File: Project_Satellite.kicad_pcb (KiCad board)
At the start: 2 copper layers, 40.2 x 65.5 mm, 83 parts, among them J1 Conn_01x02_Socket, J10 Conn_01x01_Socket, J11 Conn_01x01_Socket, J12 Conn_01x01_Socket, J13 Conn_01x01_Socket, J14 Conn_01x01_Socket, J15 Conn_01x01_Socket, J16 Conn_01x01_Socket, J17 Conn_01x01_Socket, J18 Conn_01x01_Socket, J19 Conn_01x01_Socket, J2 Conn_01x01_Socket, J20 Conn_01x01_Socket, J21 Conn_01x01_Socket, J22 Conn_01x01_Socket, J23 Conn_01x01_Socket, J24 Conn_01x01_Socket, J25 Conn_01x03_Socket, J26 Conn_01x03_Socket, J27 Conn_01x03_Socket, J28 Conn_01x03_Socket, J3 Conn_01x01_Socket, J4 Conn_01x01_Socket, J5 Conn_01x02_Socket, J6 Conn_01x02_Socket, J7 Conn_01x01_Socket, J8 Conn_01x02_Socket, J9 Conn_01x02_Socket, U3 TPS62933, U4 RASPBERRY_PI_ZERO_2_W, U5 TLV320AIC3254IRHBR, U6 MEMSMic, U7 MEMSMic, U8 TPA3118D2DAPR

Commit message: TPA3118 changes
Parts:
- removed C11: 0.1uF, Capacitor_SMD:C_0805_2012Metric_Pad1.18x1.45mm_HandSolder
- removed C7: 10uF, Capacitor_SMD:C_1206_3216Metric_Pad1.33x1.80mm_HandSolder
- removed C9: 22uF, Capacitor_SMD:C_1206_3216Metric_Pad1.33x1.80mm_HandSolder
- removed J10, J11, J12, J13, J14, J15, J16, J17, J18, J19, J2, J20, J21, J22, J23, J24, J3, J4, J7: Conn_01x01_Socket, Connector_PinHeader_2.54mm:PinHeader_1x01_P2.54mm_Vertical
- removed J27, J28: Conn_01x03_Socket, Connector_PinHeader_2.54mm:PinHeader_1x03_P2.54mm_Vertical
- removed J5, J6: Conn_01x02_Socket, Connector_PinHeader_2.54mm:PinHeader_1x02_P2.54mm_Vertical
- removed R3: 50, Resistor_SMD:R_0805_2012Metric_Pad1.20x1.40mm_HandSolder
- removed R5, R7: 10k, Resistor_SMD:R_1206_3216Metric_Pad1.30x1.75mm_HandSolder
- removed U6, U7: MEMSMic, MyFootprints:MEMSMic
- added TP2: TestPoint, TestPoint:TestPoint_Pad_D1.0mm, F.Cu at (102.2, 64.0)
- added TP3: TestPoint, TestPoint:TestPoint_Pad_D1.0mm, B.Cu at (101.0, 75.5)
- added TP4: TestPoint, TestPoint:TestPoint_Pad_D1.0mm, B.Cu at (102.2, 64.0)
- added TP5: TestPoint, TestPoint:TestPoint_Pad_D1.0mm, F.Cu at (101.0, 75.5)
- C1, C13, C19, C22, C29, C33, C34, C8, L4, L5: moved to B.Cu
- C10: value 22uF -> 47uF
- C14, C30, C31, C35, C36, C37, C38, C5, C6: moved to F.Cu
- D1: footprint Connector_PinHeader_2.54mm:PinHeader_1x02_P2.54mm_Horizontal -> LED_THT:LED_D3.0mm; moved to F.Cu
- J1, J8, J9: footprint Connector_PinHeader_2.54mm:PinHeader_1x02_P2.54mm_Vertical -> Connector_JST:JST_XH_B2B-XH-A_1x02_P2.50mm_Vertical
- J25, J26: footprint Connector_PinHeader_2.54mm:PinHeader_1x03_P2.54mm_Vertical -> Connector_JST:JST_XH_B3B-XH-A_1x03_P2.50mm_Vertical
- TP1: footprint Connector_PinHeader_2.54mm:PinHeader_1x01_P2.54mm_Horizontal -> TestPoint:TestPoint_Pad_D1.0mm
- U4: footprint Connector_PinHeader_2.54mm:PinHeader_2x20_P2.54mm_Vertical -> Connector_PinSocket_2.54mm:PinSocket_2x20_P2.54mm_Vertical
- moved J9 82.9 mm to (109.4, 115.8), turned to 0 degrees
- moved J8 78.7 mm to (100.9, 115.8), turned to 0 degrees
- moved C36 72.4 mm to (108.3, 109.8), turned to 0 degrees
- moved C37 68.4 mm to (105.4, 110.3)
- moved L3 66.9 mm to (109.4, 103.9), turned to -90 degrees
- moved C38 66.8 mm to (112.9, 110.3)
- moved C1 64.7 mm to (130.5, 67.0), turned to 180 degrees
- moved L4 63.6 mm to (103.4, 106.8), turned to -90 degrees
- moved L5 62.0 mm to (110.9, 106.8), turned to -90 degrees
- moved C35 56.8 mm to (101.4, 109.3), turned to 0 degrees
- moved C33 55.1 mm to (112.9, 96.8), turned to 180 degrees
- moved C8 53.4 mm to (103.8, 73.4), turned to -90 degrees
- moved C5 51.2 mm to (106.2, 73.0), turned to 180 degrees
- moved R2 51.0 mm to (109.0, 70.2), turned to 0 degrees
- moved L2 50.9 mm to (101.9, 103.8), turned to -90 degrees
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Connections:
- C1 pad 1: +15V -> +5V
- C12 pad 2: +3V3 -> +3.3V
- R2 pad 2: Net-(U3-FB) -> +5V
- TP1 pad 1: Net-(U5-MCLK) -> +5V
- U3 pad 2: Net-(J15-Pin_1) -> unconnected-(U3-EN-Pad2)
- U4 pad 1: +3V3 -> +3.3V
- U4 pad 11: Net-(J19-Pin_1) -> /SDZ
- U4 pad 13: Net-(J24-Pin_1) -> unconnected-(U4-GPIO27/GPIO_GEN2-Pad13)
- U4 pad 15: Net-(J20-Pin_1) -> /MUTE
- U4 pad 16: Net-(J21-Pin_1) -> /FAULTZ
- U4 pad 18: Net-(J22-Pin_1) -> unconnected-(U4-GPIO24/GPIO_GEN5-Pad18)
- U4 pad 24: Net-(J14-Pin_1) -> unconnected-(U4-GPIO8/SPI_~{CE0}-Pad24)
- U4 pad 26: Net-(J13-Pin_1) -> unconnected-(U4-GPIO7/SPI_~{CE1}-Pad26)
- U4 pad 29: Net-(J3-Pin_1) -> unconnected-(U4-GPIO5-Pad29)
- U4 pad 3: Net-(J5-Pin_2) -> /SDA
- U4 pad 31: Net-(J4-Pin_1) -> unconnected-(U4-GPIO6-Pad31)
- U4 pad 32: Net-(J16-Pin_1) -> unconnected-(U4-GPIO12-Pad32)
- U4 pad 33: Net-(J17-Pin_1) -> unconnected-(U4-GPIO13-Pad33)
- U4 pad 36: Net-(J18-Pin_1) -> /RESET
- U4 pad 37: Net-(J23-Pin_1) -> unconnected-(U4-GPIO26-Pad37)
- U4 pad 5: Net-(J5-Pin_1) -> /SCL
- U4 pad 7: Net-(J2-Pin_1) -> unconnected-(U4-GPIO4/GPIO_GCLK-Pad7)
- U5 pad 1: Net-(U5-MCLK) -> unconnected-(U5-MCLK-Pad1)
- U5 pad 10: Net-(J6-Pin_1) -> /SDA
- U5 pad 31: Net-(J7-Pin_1) -> /RESET
- U5 pad 9: Net-(J6-Pin_2) -> /SCL
- U8 pad 12: Net-(J12-Pin_1) -> /MUTE
- U8 pad 2: Net-(J10-Pin_1) -> /SDZ
- U8 pad 3: Net-(J11-Pin_1) -> /FAULTZ
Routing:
- net +15V: track 62.1 -> 7.96 mm, vias 11 -> 6
- net GND: track 91.9 -> 45.8 mm, vias 38 -> 42
- net /MUTE: track 0.00 -> 42.8 mm, vias 0 -> 3
- net /RESET: track 0.00 -> 30.8 mm, vias 0 -> 1
- net Net-(U4-GPIO18/GPIO_GEN1): track 41.0 -> 11.8 mm, vias 1 -> 0
- net Net-(J10-Pin_1): track 28.8 -> 0.00 mm, vias 2 -> 0
- net /SDZ: track 0.00 -> 28.4 mm, vias 0 -> 2
- net Net-(J16-Pin_1): track 24.3 -> 0.00 mm, vias 1 -> 0
- net /FAULTZ: track 0.00 -> 24.0 mm, vias 0 -> 1
- net /SDA: track 0.00 -> 21.0 mm
- net Net-(U4-GPIO20): track 16.0 -> 35.3 mm, vias 0 -> 3
- net Net-(J18-Pin_1): track 18.9 -> 0.00 mm
- net Net-(U4-GPIO19): track 15.3 -> 33.6 mm
- net /SCL: track 0.00 -> 18.2 mm
- net Net-(U4-GPIO21): track 20.0 -> 37.9 mm, vias 1 -> 2
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- added copper zone on In1.Cu, net +15V
- added copper zone on In1.Cu, net +3.3V
- added copper zone on In1.Cu, net +5V
- added copper zone on In2.Cu, net GND
- removed copper zone on F.Cu, net +15V
- removed copper zone on F.Cu, net +3.3V
- removed copper zone on F.Cu, net +5V
- removed copper zone on B.Cu, net GND
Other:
- board size 40.2 x 65.5 mm -> 44.5 x 61 mm
- copper layers 2 -> 4
- board text added: "Project Symphony Anjan Godavarti V2"
- board text removed: "Project Symphony Anjan Godavarti V1"

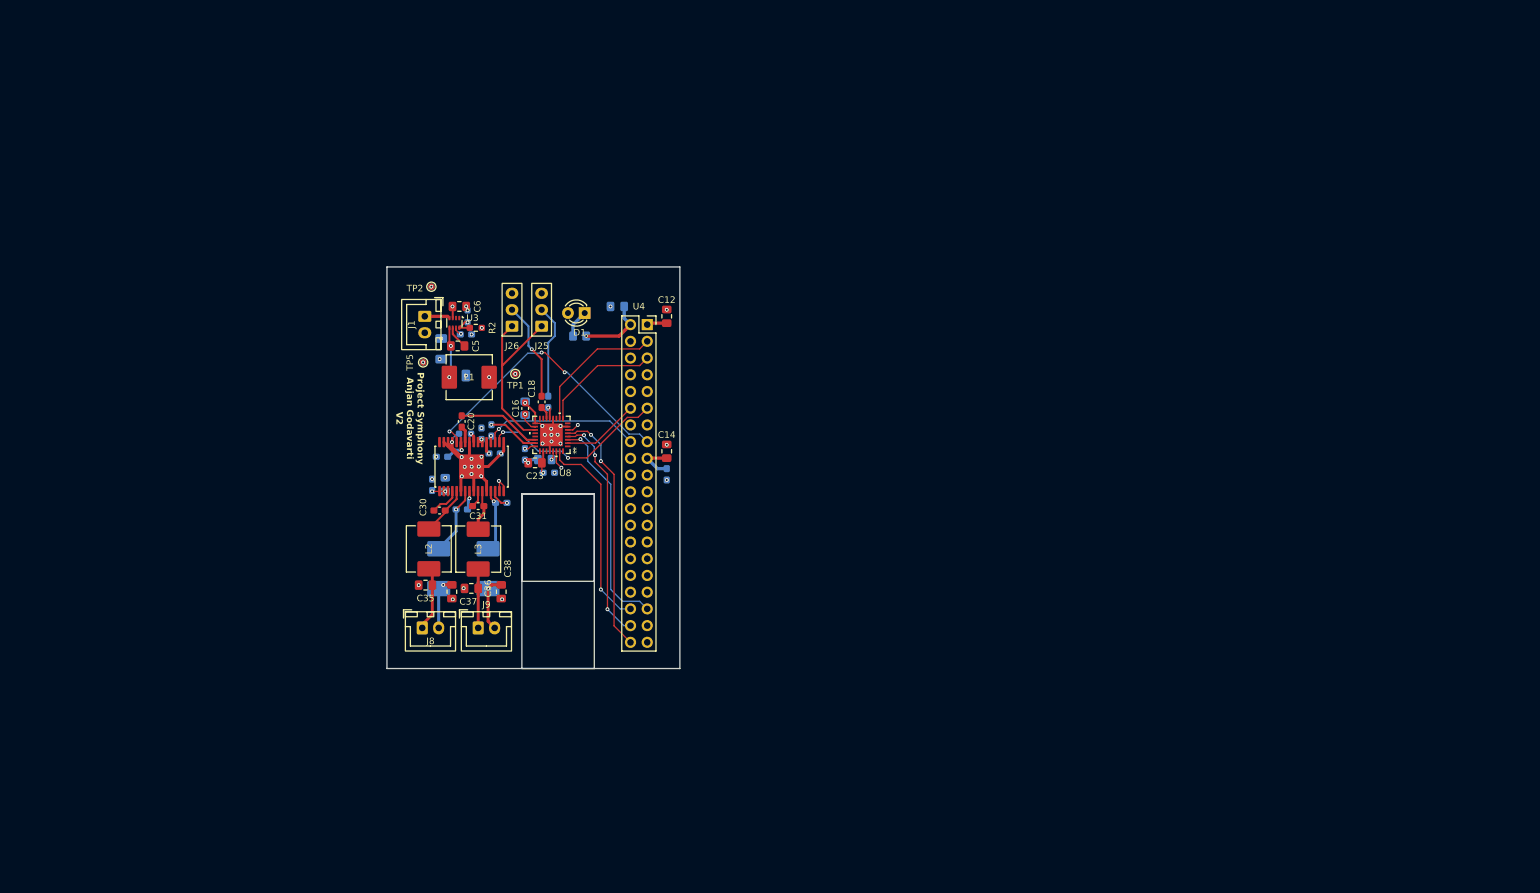
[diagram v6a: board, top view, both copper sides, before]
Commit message: Fixed V2 schematic footprints
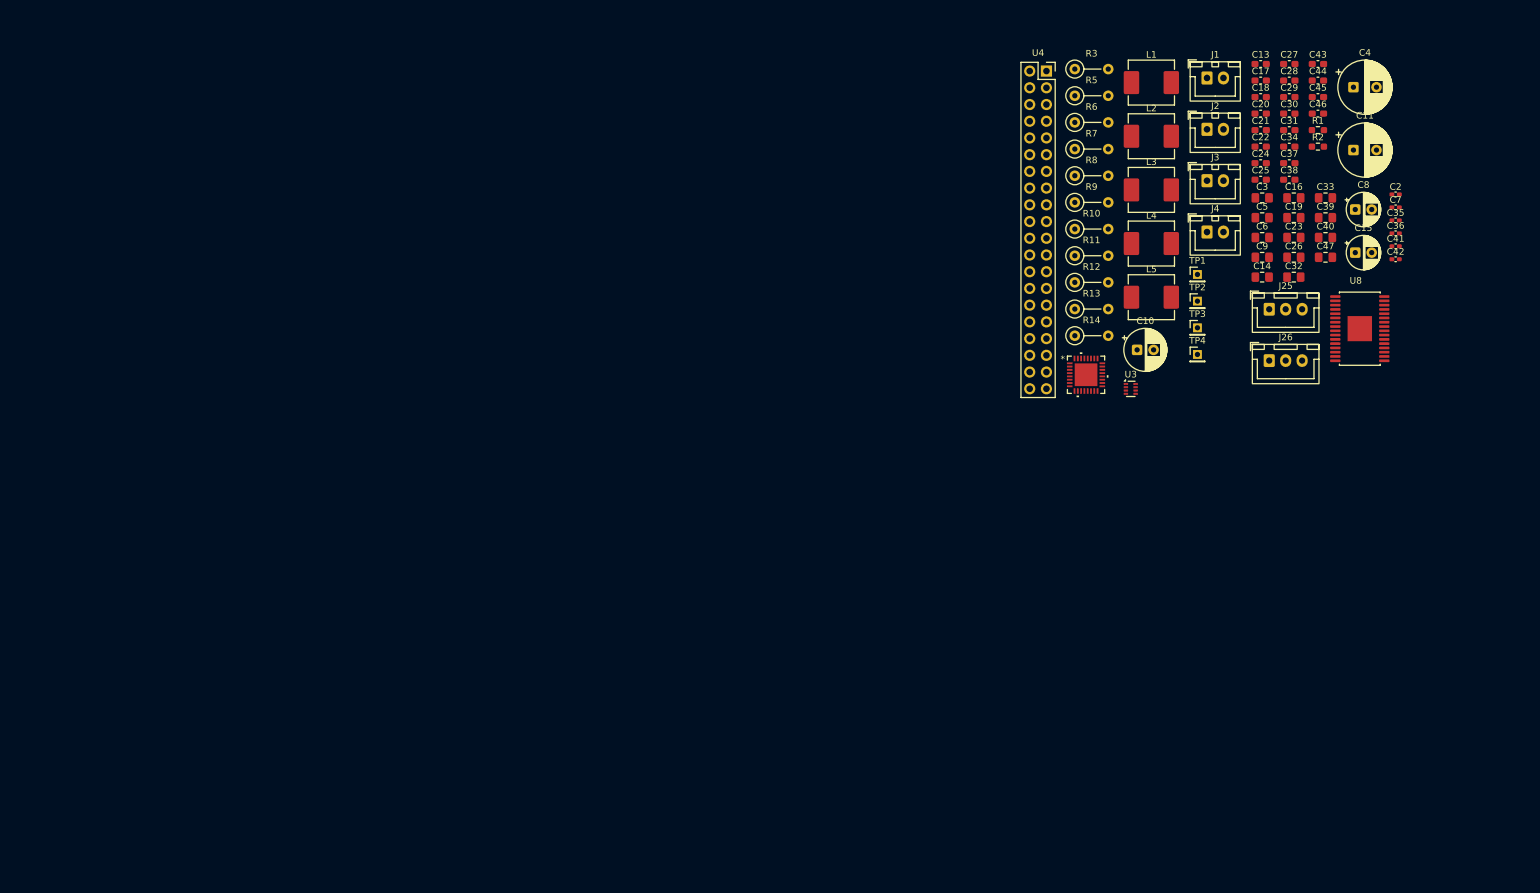
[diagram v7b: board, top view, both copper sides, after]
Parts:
- removed C1, C12: 0.1uF, Capacitor_SMD:C_0805_2012Metric_Pad1.18x1.45mm_HandSolder
- removed D1: LED, LED_THT:LED_D3.0mm
- removed J8, J9: Conn_01x02_Socket, Connector_JST:JST_XH_B2B-XH-A_1x02_P2.50mm_Vertical
- removed R4: 220, Resistor_SMD:R_0805_2012Metric_Pad1.20x1.40mm_HandSolder
- removed TP5: TestPoint, TestPoint:TestPoint_Pad_D1.0mm
- added C11: 220uF, Capacitor_THT:CP_Radial_D8.0mm_P3.50mm, F.Cu at (242.3, 43.2)
- added C2: 1nF, Capacitor_SMD:C_0402_1005Metric_Pad0.74x0.62mm_HandSolder, F.Cu at (248.7, 50.0)
- added C3: 0.1uF, Capacitor_SMD:C_0805_2012Metric_Pad1.18x1.45mm_HandSolder, F.Cu at (228.4, 50.5)
- added C39: 680nF, Capacitor_SMD:C_0805_2012Metric_Pad1.18x1.45mm_HandSolder, F.Cu at (238.1, 53.5)
- added C4: 220uF, Capacitor_THT:CP_Radial_D8.0mm_P3.50mm, F.Cu at (242.3, 33.7)
- added C40: 680nF, Capacitor_SMD:C_0805_2012Metric_Pad1.18x1.45mm_HandSolder, F.Cu at (238.1, 56.5)
- added C41: 1nF, Capacitor_SMD:C_0402_1005Metric_Pad0.74x0.62mm_HandSolder, F.Cu at (248.7, 57.9)
- added C42: 1nF, Capacitor_SMD:C_0402_1005Metric_Pad0.74x0.62mm_HandSolder, F.Cu at (248.7, 59.8)
- added C43: 10nF, Capacitor_SMD:C_0603_1608Metric_Pad1.08x0.95mm_HandSolder, F.Cu at (236.9, 30.2)
- added C44: 10nF, Capacitor_SMD:C_0603_1608Metric_Pad1.08x0.95mm_HandSolder, F.Cu at (236.9, 32.7)
- added C45: 220nF, Capacitor_SMD:C_0603_1608Metric_Pad1.08x0.95mm_HandSolder, F.Cu at (236.9, 35.2)
- added C46: 220nF, Capacitor_SMD:C_0603_1608Metric_Pad1.08x0.95mm_HandSolder, F.Cu at (236.9, 37.7)
- added C47: 0.1uF, Capacitor_SMD:C_0805_2012Metric_Pad1.18x1.45mm_HandSolder, F.Cu at (238.1, 59.5)
- added C7: 1nF, Capacitor_SMD:C_0402_1005Metric_Pad0.74x0.62mm_HandSolder, F.Cu at (248.7, 52.0)
- added C9: 0.1uF, Capacitor_SMD:C_0805_2012Metric_Pad1.18x1.45mm_HandSolder, F.Cu at (228.4, 59.5)
- added J2: Conn_01x02_Socket, Connector_JST:JST_XH_B2B-XH-A_1x02_P2.50mm_Vertical, F.Cu at (220.1, 40.1)
- added J3: Conn_01x02_Socket, Connector_JST:JST_XH_B2B-XH-A_1x02_P2.50mm_Vertical, F.Cu at (220.1, 47.9)
- added J4: Conn_01x02_Socket, Connector_JST:JST_XH_B2B-XH-A_1x02_P2.50mm_Vertical, F.Cu at (220.1, 55.7)
- added R10: 3.3, Resistor_THT:R_Axial_DIN0207_L6.3mm_D2.5mm_P5.08mm_Vertical, F.Cu at (200.0, 55.2)
- added R11: 3.3, Resistor_THT:R_Axial_DIN0207_L6.3mm_D2.5mm_P5.08mm_Vertical, F.Cu at (200.0, 59.3)
- added R12: 3.3, Resistor_THT:R_Axial_DIN0207_L6.3mm_D2.5mm_P5.08mm_Vertical, F.Cu at (200.0, 63.3)
- added R13: 10k, Resistor_THT:R_Axial_DIN0207_L6.3mm_D2.5mm_P5.08mm_Vertical, F.Cu at (200.0, 67.4)
- added R14: 4.7k, Resistor_THT:R_Axial_DIN0207_L6.3mm_D2.5mm_P5.08mm_Vertical, F.Cu at (200.0, 71.4)
- added R3: 100k, Resistor_THT:R_Axial_DIN0207_L6.3mm_D2.5mm_P5.08mm_Vertical, F.Cu at (200.0, 30.9)
- added R5: 3.3, Resistor_THT:R_Axial_DIN0207_L6.3mm_D2.5mm_P5.08mm_Vertical, F.Cu at (200.0, 35.0)
- added R7: 20k, Resistor_THT:R_Axial_DIN0207_L6.3mm_D2.5mm_P5.08mm_Vertical, F.Cu at (200.0, 43.1)
- added R8: 100k, Resistor_THT:R_Axial_DIN0207_L6.3mm_D2.5mm_P5.08mm_Vertical, F.Cu at (200.0, 47.1)
- added R9: 3.3, Resistor_THT:R_Axial_DIN0207_L6.3mm_D2.5mm_P5.08mm_Vertical, F.Cu at (200.0, 51.2)
- C10: footprint Capacitor_SMD:C_1206_3216Metric_Pad1.33x1.80mm_HandSolder -> Capacitor_THT:CP_Radial_D6.3mm_P2.50mm; moved to F.Cu
- C13: value 1uF -> 10uF; moved to F.Cu
- C15: value 0.1uF -> 10uF; footprint Capacitor_SMD:C_0805_2012Metric_Pad1.18x1.45mm_HandSolder -> Capacitor_THT:CP_Radial_D5.0mm_P2.50mm; moved to F.Cu
- C16: value 1uF -> 0.1uF; footprint Capacitor_SMD:C_0603_1608Metric_Pad1.08x0.95mm_HandSolder -> Capacitor_SMD:C_0805_2012Metric_Pad1.18x1.45mm_HandSolder
- C17, C24, C25, C27, C29, C34, L4, L5, R1: moved to F.Cu
- C19: value 2.2uF -> 0.1uF; footprint Capacitor_SMD:C_0603_1608Metric_Pad1.08x0.95mm_HandSolder -> Capacitor_SMD:C_0805_2012Metric_Pad1.18x1.45mm_HandSolder; moved to F.Cu
- C20: value 2.2uF -> 10nF
- C21, C22: value 2.2uF -> 1uF; moved to F.Cu
- C26: value 0.1uF -> 1uF; moved to F.Cu
- C28: value 0.1uF -> 1uF; footprint Capacitor_SMD:C_0805_2012Metric_Pad1.18x1.45mm_HandSolder -> Capacitor_SMD:C_0603_1608Metric_Pad1.08x0.95mm_HandSolder; moved to F.Cu
- C32, C33: value 220nF -> 680nF; footprint Capacitor_SMD:C_0603_1608Metric_Pad1.08x0.95mm_HandSolder -> Capacitor_SMD:C_0805_2012Metric_Pad1.18x1.45mm_HandSolder; moved to F.Cu
- C35, C36: value 680nF -> 1nF; footprint Capacitor_SMD:C_0805_2012Metric_Pad1.18x1.45mm_HandSolder -> Capacitor_SMD:C_0402_1005Metric_Pad0.74x0.62mm_HandSolder
- C37, C38: value 680nF -> 10nF; footprint Capacitor_SMD:C_0805_2012Metric_Pad1.18x1.45mm_HandSolder -> Capacitor_SMD:C_0603_1608Metric_Pad1.08x0.95mm_HandSolder
- C8: footprint Capacitor_SMD:C_1206_3216Metric_Pad1.33x1.80mm_HandSolder -> Capacitor_THT:CP_Radial_D5.0mm_P2.50mm; moved to F.Cu
- R6: value 5.6k -> 100k; footprint Resistor_SMD:R_0603_1608Metric_Pad0.98x0.95mm_HandSolder -> Resistor_THT:R_Axial_DIN0207_L6.3mm_D2.5mm_P5.08mm_Vertical; moved to F.Cu
- TP1, TP2: footprint TestPoint:TestPoint_Pad_D1.0mm -> Connector_PinHeader_2.00mm:PinHeader_1x01_P2.00mm_Vertical
- TP3, TP4: footprint TestPoint:TestPoint_Pad_D1.0mm -> Connector_PinHeader_2.00mm:PinHeader_1x01_P2.00mm_Vertical; moved to F.Cu
- moved C35 157.4 mm to (248.7, 53.9)
- moved C36 150.4 mm to (248.7, 55.9)
- moved C29 142.9 mm to (232.6, 35.2), turned to 0 degrees
- moved C37 142.9 mm to (232.6, 45.2), turned to 0 degrees
- moved C30 142.5 mm to (232.6, 37.7), turned to 0 degrees
- moved C28 142.1 mm to (232.6, 32.7), turned to 0 degrees
- moved C8 140.4 mm to (242.6, 52.3), turned to 0 degrees
- moved U8 136.5 mm to (243.3, 70.4), turned to 0 degrees
- moved C31 135.8 mm to (232.6, 40.2)
- moved C38 135.1 mm to (232.6, 47.7), turned to 0 degrees
- moved C27 134.9 mm to (232.6, 30.2), turned to 0 degrees
- moved C19 134.4 mm to (233.3, 53.5)
- moved C33 133.5 mm to (238.1, 50.5), turned to 0 degrees
- moved R1 132.2 mm to (236.9, 40.2), turned to 0 degrees
- moved C32 131.2 mm to (233.3, 62.5), turned to 0 degrees
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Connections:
- C16 pad 1: Net-(U5-REF) -> Net-(J26-Pin_1)
- C16 pad 2: GND -> +3.3V
- C19 pad 1: GND -> Net-(C19-Pad1)
- C19 pad 2: Net-(U8-LINN) -> GND
- C20 pad 1: Net-(U5-LOL) -> +15V
- C20 pad 2: Net-(U8-LINP) -> GND
- C21 pad 1: GND -> Net-(U5-LOR)
- C21 pad 2: Net-(U8-RINN) -> Net-(U8-RINP)
- C22 pad 1: Net-(U5-LOR) -> GND
- C22 pad 2: Net-(U8-RINP) -> Net-(U8-RINN)
- C27 pad 1: Net-(U8-GVDD) -> GND
- C27 pad 2: GND -> Net-(U8-GVDD)
- C28 pad 1: GND -> Net-(U5-LOL)
- C28 pad 2: +15V -> Net-(U8-LINP)
- C29 pad 2: +15V -> Net-(U8-LINN)
- C30 pad 1: Net-(U8-OUTNL) -> Net-(U8-BSPR)
- C30 pad 2: Net-(U8-BSNL) -> Net-(U8-OUTPR)
- C32 pad 1: Net-(U8-BSPL) -> GND
- C32 pad 2: Net-(U8-OUTPL) -> Net-(C32-Pad2)
- C33 pad 1: Net-(U8-BSPR) -> Net-(C33-Pad1)
- C33 pad 2: Net-(U8-OUTPR) -> GND
- C35 pad 1: GND -> Net-(C33-Pad1)
- C35 pad 2: Net-(J8-Pin_1) -> GND
- C36 pad 2: Net-(J9-Pin_1) -> Net-(C32-Pad2)
- C37 pad 1: Net-(J8-Pin_2) -> Net-(J2-Pin_1)
- C38 pad 1: Net-(J9-Pin_2) -> GND
- C38 pad 2: GND -> Net-(J2-Pin_2)
- J25 pad 1: /MICBIAS -> Net-(J25-Pin_1)
- J26 pad 1: /MICBIAS -> Net-(J26-Pin_1)
- L2 pad 1: Net-(U8-OUTNL) -> Net-(U8-OUTPR)
- L2 pad 2: Net-(J8-Pin_1) -> Net-(C33-Pad1)
- L3 pad 2: Net-(J9-Pin_1) -> Net-(C32-Pad2)
- L4 pad 2: Net-(J8-Pin_2) -> Net-(C39-Pad1)
- L5 pad 1: Net-(U8-OUTPR) -> Net-(U8-OUTNL)
- L5 pad 2: Net-(J9-Pin_2) -> Net-(C40-Pad2)
- R6 pad 1: GND -> Net-(U8-GVDD)
- U4 pad 1: +3.3V -> unconnected-(U4-3V3_1-Pad1)
- U4 pad 16: /FAULTZ -> unconnected-(U4-GPIO23/GPIO_GEN4-Pad16)
- U4 pad 17: +3.3V -> unconnected-(U4-3V3_17-Pad17)
- U4 pad 2: +5V -> unconnected-(U4-5V_2-Pad2)
- U4 pad 4: +5V -> unconnected-(U4-5V_4-Pad4)
- U5 pad 12: GND -> Net-(U5-SPI_SELECT)
- U5 pad 19: /MICBIAS -> unconnected-(U5-MICBIAS-Pad19)
- U5 pad 30: +3.3V -> Net-(U5-LDO_SELECT)
- U8 pad 17: +15V -> Net-(U8-AVCC)
- U8 pad 18: +15V -> Net-(U8-AVCC)
- U8 pad 19: +15V -> Net-(U8-AVCC)
- U8 pad 3: /FAULTZ -> /SDZ
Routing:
- net GND: track 45.8 -> 0.00 mm, vias 42 -> 0
- net /MUTE: track 42.8 -> 0.00 mm, vias 3 -> 0
- net Net-(U4-GPIO21): track 37.9 -> 0.00 mm, vias 2 -> 0
- net Net-(U4-GPIO20): track 35.3 -> 0.00 mm, vias 3 -> 0
- net Net-(U4-GPIO19): track 33.6 -> 0.00 mm, vias 1 -> 0
- net /RESET: track 30.8 -> 0.00 mm, vias 1 -> 0
- net /SDZ: track 28.4 -> 0.00 mm, vias 2 -> 0
- net /MICBIAS: track 28.0 -> 0.00 mm
- net /FAULTZ: track 24.0 -> 0.00 mm, vias 1 -> 0
- net /SDA: track 21.0 -> 0.00 mm
- net /SCL: track 18.2 -> 0.00 mm
- net +3.3V: track 17.8 -> 0.00 mm, vias 3 -> 0
- net Net-(J26-Pin_2): track 15.0 -> 0.00 mm, vias 1 -> 0
- net Net-(J25-Pin_2): track 14.4 -> 0.00 mm
- net Net-(U5-LOL): track 12.7 -> 0.00 mm
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- removed copper zone on In1.Cu, net +15V
- removed copper zone on In1.Cu, net +3.3V
- removed copper zone on In1.Cu, net +5V
- removed copper zone on In2.Cu, net GND
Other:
- board outline removed
- board text removed: "Project Symphony Anjan Godavarti V2"

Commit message: V2 PCB Placement and Plane Placement
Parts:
- removed TP4: TestPoint, Connector_PinHeader_2.00mm:PinHeader_1x01_P2.00mm_Vertical
- C13: footprint Capacitor_SMD:C_0603_1608Metric_Pad1.08x0.95mm_HandSolder -> Capacitor_THT:CP_Radial_D5.0mm_P2.50mm
- C14, C16, C18, C19, C2, C21, C23, C27, C28, C31, C34, C35, C36, C37, C38, C41, C42, C43, C44, C46, C47, C6, C9, L1, L2, L3, L4, L5, TP3: moved to B.Cu
- moved C47 207.5 mm to (44.2, 133.5), turned to 180 degrees
- moved C13 206.0 mm to (44.7, 123.8), turned to 180 degrees
- moved C17 200.5 mm to (50.4, 125.3), turned to 90 degrees
- moved C18 198.2 mm to (51.7, 125.3), turned to -90 degrees
- moved C15 197.6 mm to (55.4, 122.3)
- moved C16 197.3 mm to (55.5, 136.2), turned to -90 degrees
- moved J25 196.5 mm to (45.2, 135.8)
- moved C8 192.9 mm to (75.3, 148.2), turned to -90 degrees
- moved C14 192.7 mm to (45.1, 121.8), turned to 180 degrees
- moved C27 192.7 mm to (62.1, 120.0)
- moved C28 192.2 mm to (62.1, 121.5)
- moved C29 191.7 mm to (62.1, 123.0)
- moved C26 191.1 mm to (50.4, 115.0), turned to -90 degrees
- moved C23 189.4 mm to (53.4, 116.0), turned to 180 degrees
- moved C24 189.2 mm to (52.4, 115.0), turned to -90 degrees
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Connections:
- U4 pad 1: unconnected-(U4-3V3_1-Pad1) -> +3.3V
- U4 pad 17: unconnected-(U4-3V3_17-Pad17) -> +3.3V
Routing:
- added copper zone on In1.Cu, net +15V
- added copper zone on In1.Cu, net +3.3V
- added copper zone on In1.Cu, net +5V
- added copper zone on In2.Cu, net GND
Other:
- board outline added: 63.8 x 61 mm
